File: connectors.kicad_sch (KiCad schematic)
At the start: 4 parts, among them J1 Conn_01x04_Pin, J2 Conn_01x09_Pin, J3 Conn_01x04_Pin, J4 Conn_02x03_Odd_Even

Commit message: Completed symbol—footprint associations.
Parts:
- J1, J3: footprint (none) -> Connector_PinHeader_2.54mm:PinHeader_1x04_P2.54mm_Vertical
- J2: footprint (none) -> Connector_PinHeader_2.54mm:PinHeader_1x09_P2.54mm_Vertical
- J4: footprint (none) -> Connector_PinHeader_2.54mm:PinHeader_2x03_P2.54mm_Vertical
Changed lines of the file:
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@@
 			)
 		)
-		(property "Footprint" ""
+		(property "Footprint" "Connector_PinHeader_2.54mm:PinHeader_1x04_P2.54mm_Vertical"
 			(at 110.49 62.23 0)
 			(effects
@@
 			)
 		)
-		(property "Footprint" ""
+		(property "Footprint" "Connector_PinHeader_2.54mm:PinHeader_1x09_P2.54mm_Vertical"
 			(at 86.36 90.17 0)
 			(effects
@@
 			)
 		)
-		(property "Footprint" ""
+		(property "Footprint" "Connector_PinHeader_2.54mm:PinHeader_2x03_P2.54mm_Vertical"
 			(at 113.03 86.36 0)
 			(effects
@@
 			)
 		)
-		(property "Footprint" ""
+		(property "Footprint" "Connector_PinHeader_2.54mm:PinHeader_1x04_P2.54mm_Vertical"
 			(at 86.36 62.23 0)
 			(effects

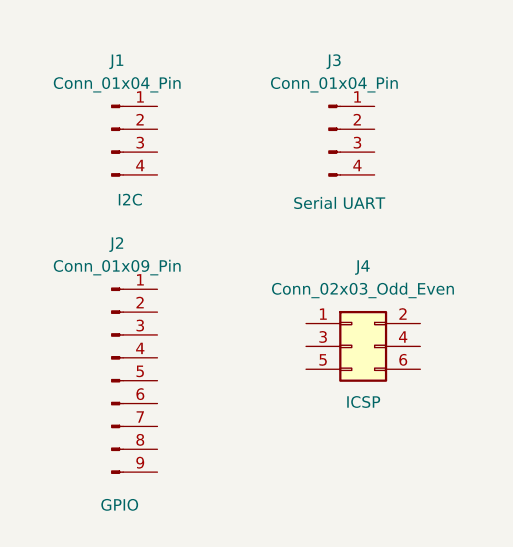
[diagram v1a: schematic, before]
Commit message: Allocated GND and Vcc nets to the Power net class.
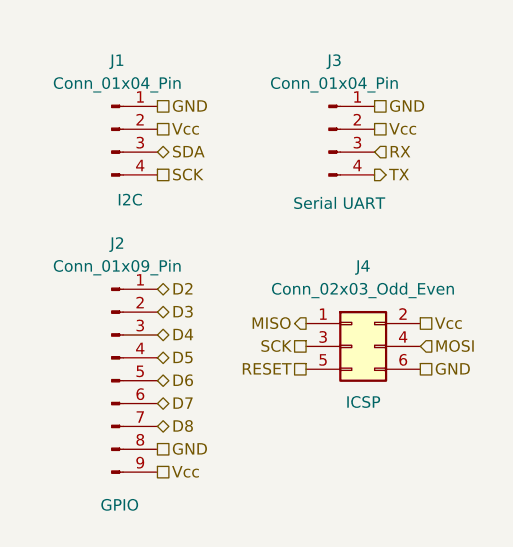
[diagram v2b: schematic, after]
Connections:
- net GND: now reaches J3.1 (Pin_1)
- net GND: now also J1.1 (Pin_1), J2.8 (Pin_8), J4.6 (Pin_6)
- net Vcc: now reaches J3.2 (Pin_2)
- net Vcc: now also J1.2 (Pin_2), J2.9 (Pin_9), J4.2 (Pin_2)
- net RX: now reaches J3.3 (Pin_3)
- net TX: now reaches J3.4 (Pin_4)
- net D2: now reaches J2.1 (Pin_1)
- net D3: now reaches J2.2 (Pin_2)
- net D4: now reaches J2.3 (Pin_3)
- net D5: now reaches J2.4 (Pin_4)
- net D6: now reaches J2.5 (Pin_5)
- net D7: now reaches J2.6 (Pin_6)
- net D8: now reaches J2.7 (Pin_7)
- net MISO: now reaches J4.1 (Pin_1)
- net SCK: now reaches J4.3 (Pin_3)
- net SCK: now also J1.4 (Pin_4)
- net MOSI: now reaches J4.4 (Pin_4)
- net RESET: now reaches J4.5 (Pin_5)
- net SDA: now reaches J1.3 (Pin_3)

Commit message: Completed comments.
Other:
- note added: "Connectors"
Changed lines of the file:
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@@
 	(generator_version "8.0")
 	(paper "A4")
+	(rectangle
+		(start 77.47 52.705)
+		(end 128.905 106.68)
+		(stroke
+			(width 0)
+			(type dot)
+		)
+		(fill
+			(type none)
+		)
+	)
+	(text "Connectors"
+		(exclude_from_sim no)
+		(at 82.296 51.435 0)
+		(effects
+			(font
+				(size 1.27 1.27)
+			)
+		)
+	)
 	(hierarchical_label "TX"
 		(shape output)

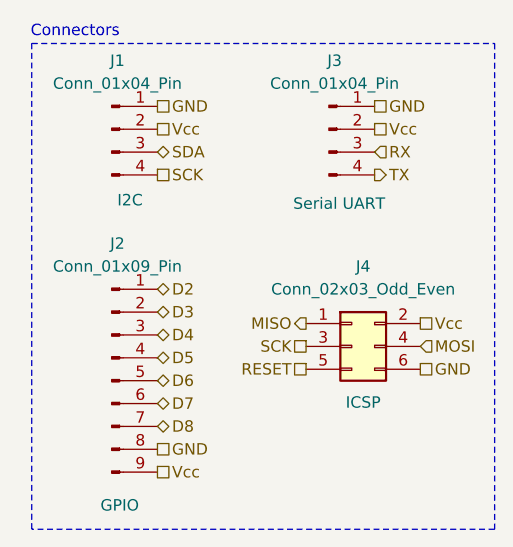
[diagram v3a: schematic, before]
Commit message: Fixed issue with I2C SCL.
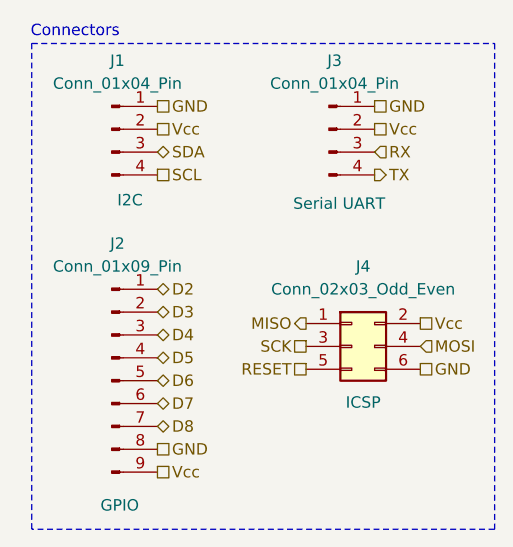
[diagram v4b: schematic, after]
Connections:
- net SCK: no longer J1.4 (Pin_4)
- new net SCL: J1.4 (Pin_4)
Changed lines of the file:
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@@
 (kicad_sch
-	(version 20231120)
+	(version 20250114)
 	(generator "eeschema")
-	(generator_version "8.0")
+	(generator_version "9.0")
 	(paper "A4")
 	(rectangle
@@
 		(shape output)
 		(at 115.57 67.31 0)
-		(fields_autoplaced yes)
 		(effects
 			(font
@@
 		(shape passive)
 		(at 91.44 59.69 0)
-		(fields_autoplaced yes)
 		(effects
 			(font
@@
 		(shape input)
 		(at 120.65 86.36 0)
-		(fields_autoplaced yes)
 		(effects
 			(font
@@
 		(shape bidirectional)
 		(at 91.44 82.55 0)
-		(fields_autoplaced yes)
 		(effects
 			(font
@@
 		(shape bidirectional)
 		(at 91.44 85.09 0)
-		(fields_autoplaced yes)
 		(effects
 			(font
@@
 		(shape passive)
 		(at 115.57 59.69 0)
-		(fields_autoplaced yes)
 		(effects
 			(font
@@
 		(shape passive)
 		(at 91.44 97.79 0)
-		(fields_autoplaced yes)
 		(effects
 			(font
@@
 		(shape passive)
 		(at 115.57 62.23 0)
-		(fields_autoplaced yes)
 		(effects
 			(font
@@
 		(shape passive)
 		(at 107.95 86.36 180)
-		(fields_autoplaced yes)
 		(effects
 			(font
@@
 		(shape bidirectional)
 		(at 91.44 64.77 0)
-		(fields_autoplaced yes)
 		(effects
 			(font
@@
 		(shape bidirectional)
 		(at 91.44 80.01 0)
-		(fields_autoplaced yes)
 		(effects
 			(font
@@
 		(shape passive)
 		(at 91.44 62.23 0)
-		(fields_autoplaced yes)
 		(effects
 			(font
@@
 		(shape passive)
 		(at 91.44 100.33 0)
-		(fields_autoplaced yes)
 		(effects
 			(font
@@
 		(shape bidirectional)
 		(at 91.44 87.63 0)
-		(fields_autoplaced yes)
 		(effects
 			(font
@@
 		(shape bidirectional)
 		(at 91.44 95.25 0)
-		(fields_autoplaced yes)
 		(effects
 			(font
@@
 		(shape bidirectional)
 		(at 91.44 90.17 0)
-		(fields_autoplaced yes)
 		(effects
 			(font
@@
 		(shape bidirectional)
 		(at 91.44 92.71 0)
-		(fields_autoplaced yes)
 		(effects
 			(font
@@
 		(shape passive)
 		(at 120.65 88.9 0)
-		(fields_autoplaced yes)
 		(effects
 			(font
@@
 		(shape input)
 		(at 115.57 64.77 0)
-		(fields_autoplaced yes)
 		(effects
 			(font
@@
 		(shape passive)
 		(at 107.95 88.9 180)
-		(fields_autoplaced yes)
 		(effects
 			(font
@@
 		(shape output)
 		(at 107.95 83.82 180)
-		(fields_autoplaced yes)
 		(effects
 			(font
@@
 		(shape passive)
 		(at 120.65 83.82 0)
-		(fields_autoplaced yes)
-		(effects
-			(font
-				(size 1.27 1.27)
-			)
-			(justify left)
-		)
-	)
-	(hierarchical_label "SCK"
+		(effects
+			(font
+				(size 1.27 1.27)
+			)
+			(justify left)
+		)
+	)
+	(hierarchical_label "SCL"
 		(shape passive)
 		(at 91.44 67.31 0)
-		(fields_autoplaced yes)
-		(effects
-			(font
+		(effects
+			(font
